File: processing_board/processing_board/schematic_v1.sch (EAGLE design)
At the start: 20 parts, among them Q1 BSS138, Q2 BSS138

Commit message: modified shcematic and board
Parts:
- added J3: (no value), SparkFun-Connectors:CONN_04PTH
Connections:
- removed net N$11: Q2.S, R3.1
- removed net N$2: Q1.S, R2.1
- removed net VDD: C2.1, C3.2, U$1.VIN
- new net CAN_RX: J3.3, Q1.S, R2.1
- new net CAN_TX: J3.2, Q2.S, R3.1
- net +5V: now also C2.1, C3.2, J3.1, U$1.VIN
- net GND: now also J3.4
- net TEENSY_3.3V: now also U$1.3.3V
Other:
- note added: "Level converters from CAN controller to CAN transiever"
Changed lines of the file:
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@@
 <part name="PWR6" library="supply" deviceset="+5V" device=""/>
 <part name="PWR7" library="supply" deviceset="+5V" device=""/>
+<part name="PWR8" library="supply" deviceset="+5V" device=""/>
+<part name="J3" library="SparkFun-Connectors" deviceset="CONN_04" device="PTH"/>
+<part name="GND8" library="supply" deviceset="GND" device=""/>
+<part name="PWR9" library="supply" deviceset="+5V" device=""/>
 </parts>
 <sheets>
@@
 <plain>
 <text x="62.23" y="63.5" size="1.778" layer="91">Supply Decoupling</text>
+<text x="-96.52" y="30.48" size="1.778" layer="91">Level converters from CAN controller to CAN transiever</text>
 </plain>
 <instances>
@@
 <instance part="PWR6" gate="G$1" x="-86.36" y="93.98" smashed="yes"/>
 <instance part="PWR7" gate="G$1" x="-88.9" y="63.5" smashed="yes" rot="R90"/>
+<instance part="PWR8" gate="G$1" x="60.96" y="73.66" smashed="yes" rot="R270"/>
+<instance part="J3" gate="J1" x="-121.92" y="55.88" smashed="yes">
+<attribute name="VALUE" x="-127" y="48.514" size="1.778" layer="96" font="vector"/>
+<attribute name="NAME" x="-127" y="64.008" size="1.778" layer="95" font="vector"/>
+</instance>
+<instance part="GND8" gate="VR1" x="-109.22" y="68.58" smashed="yes" rot="R180"/>
+<instance part="PWR9" gate="G$1" x="-109.22" y="45.72" smashed="yes" rot="R180"/>
 </instances>
 <busses>
 </busses>
 <nets>
-<net name="VDD" class="0">
-<segment>
-<pinref part="C3" gate="G$1" pin="2"/>
-<wire x1="55.88" y1="54.356" x2="55.88" y2="53.34" width="0.1524" layer="91"/>
-<wire x1="55.88" y1="53.34" x2="55.88" y2="45.72" width="0.1524" layer="91"/>
-<wire x1="63.5" y1="45.72" x2="55.88" y2="45.72" width="0.1524" layer="91"/>
-<pinref part="C2" gate="G$1" pin="1"/>
-<wire x1="62.738" y1="54.356" x2="55.88" y2="54.356" width="0.1524" layer="91"/>
-<pinref part="U$1" gate="G$1" pin="VIN"/>
-<wire x1="44.45" y1="68.58" x2="55.88" y2="68.58" width="0.1524" layer="91"/>
-<wire x1="55.88" y1="68.58" x2="55.88" y2="54.356" width="0.1524" layer="91"/>
-</segment>
-</net>
 <net name="GND" class="0">
 <segment>
@@
 <wire x1="200.66" y1="45.72" x2="200.66" y2="48.26" width="0.1524" layer="91"/>
 </segment>
+<segment>
+<pinref part="J3" gate="J1" pin="4"/>
+<wire x1="-116.84" y1="60.96" x2="-109.22" y2="60.96" width="0.1524" layer="91"/>
+<wire x1="-109.22" y1="60.96" x2="-109.22" y2="66.04" width="0.1524" layer="91"/>
+<pinref part="GND8" gate="VR1" pin="GND"/>
+</segment>
 </net>
 <net name="+15V" class="0">
@@
 <wire x1="-88.9" y1="63.5" x2="-86.36" y2="63.5" width="0.1524" layer="91"/>
 </segment>
+<segment>
+<pinref part="PWR8" gate="G$1" pin="+5V"/>
+<wire x1="60.96" y1="73.66" x2="58.42" y2="73.66" width="0.1524" layer="91"/>
+<wire x1="58.42" y1="73.66" x2="58.42" y2="68.58" width="0.1524" layer="91"/>
+<pinref part="C3" gate="G$1" pin="2"/>
+<wire x1="55.88" y1="54.356" x2="55.88" y2="45.72" width="0.1524" layer="91"/>
+<wire x1="63.5" y1="45.72" x2="55.88" y2="45.72" width="0.1524" layer="91"/>
+<pinref part="C2" gate="G$1" pin="1"/>
+<wire x1="62.738" y1="54.356" x2="55.88" y2="54.356" width="0.1524" layer="91"/>
+<pinref part="U$1" gate="G$1" pin="VIN"/>
+<wire x1="44.45" y1="68.58" x2="53.34" y2="68.58" width="0.1524" layer="91"/>
+<wire x1="53.34" y1="68.58" x2="55.88" y2="68.58" width="0.1524" layer="91"/>
+<wire x1="55.88" y1="68.58" x2="55.88" y2="54.356" width="0.1524" layer="91"/>
+<wire x1="58.42" y1="68.58" x2="55.88" y2="68.58" width="0.1524" layer="91"/>
+</segment>
+<segment>
+<pinref part="J3" gate="J1" pin="1"/>
+<wire x1="-116.84" y1="53.34" x2="-109.22" y2="53.34" width="0.1524" layer="91"/>
+<wire x1="-109.22" y1="53.34" x2="-109.22" y2="45.72" width="0.1524" layer="91"/>
+<pinref part="PWR9" gate="G$1" pin="+5V"/>
+</segment>
 </net>
 <net name="+3.3V" class="0">
@@
 </segment>
 </net>
-<net name="N$2" class="0">
+<net name="CAN_RX" class="0">
 <segment>
 <pinref part="R2" gate="G$1" pin="1"/>
@@
 <wire x1="-86.36" y1="68.58" x2="-96.52" y2="68.58" width="0.1524" layer="91"/>
 <junction x="-86.36" y="68.58"/>
+<pinref part="J3" gate="J1" pin="3"/>
+<wire x1="-116.84" y1="58.42" x2="-96.52" y2="58.42" width="0.1524" layer="91"/>
+<wire x1="-96.52" y1="58.42" x2="-96.52" y2="68.58" width="0.1524" layer="91"/>
+<label x="-99.06" y="60.96" size="1.778" layer="95" rot="R180"/>
 </segment>
 </net>
@@
 <label x="-63.5" y="60.96" size="1.778" layer="95"/>
 </segment>
-</net>
-<net name="N$11" class="0">
+<segment>
+<pinref part="U$1" gate="G$1" pin="3.3V"/>
+<wire x1="-1.27" y1="30.48" x2="-10.16" y2="30.48" width="0.1524" layer="91"/>
+<label x="-10.16" y="30.48" size="1.778" layer="95" rot="R180"/>
+</segment>
+</net>
+<net name="CAN_TX" class="0">
 <segment>
 <pinref part="R3" gate="G$1" pin="1"/>
@@
 <wire x1="-86.36" y1="40.64" x2="-96.52" y2="40.64" width="0.1524" layer="91"/>
 <junction x="-86.36" y="40.64"/>
-</segment>
-</net>
+<wire x1="-96.52" y1="40.64" x2="-96.52" y2="55.88" width="0.1524" layer="91"/>
+<pinref part="J3" gate="J1" pin="2"/>
+<wire x1="-96.52" y1="55.88" x2="-116.84" y2="55.88" width="0.1524" layer="91"/>
+<label x="-99.06" y="55.88" size="1.778" layer="95" rot="R180"/>
+</segment>
+</net>

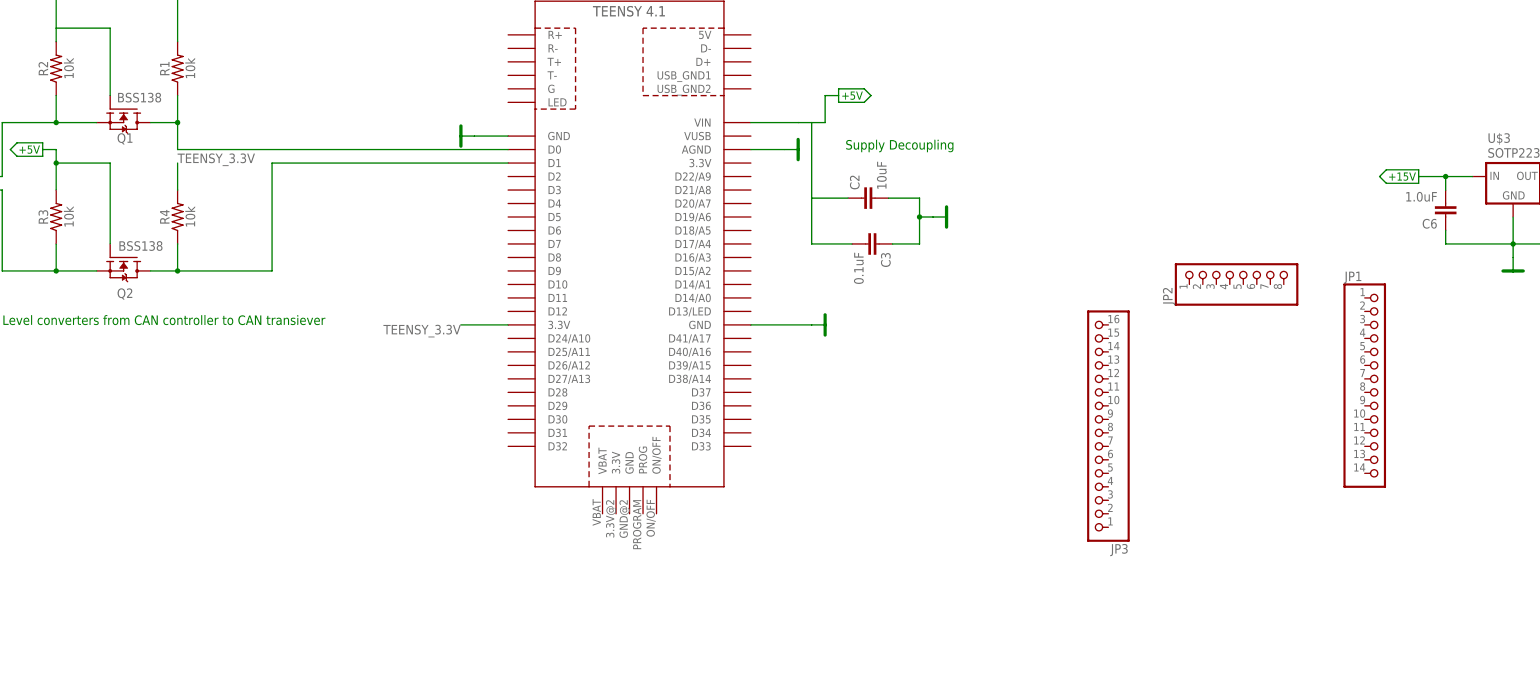
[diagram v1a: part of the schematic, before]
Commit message: routed to radio mod
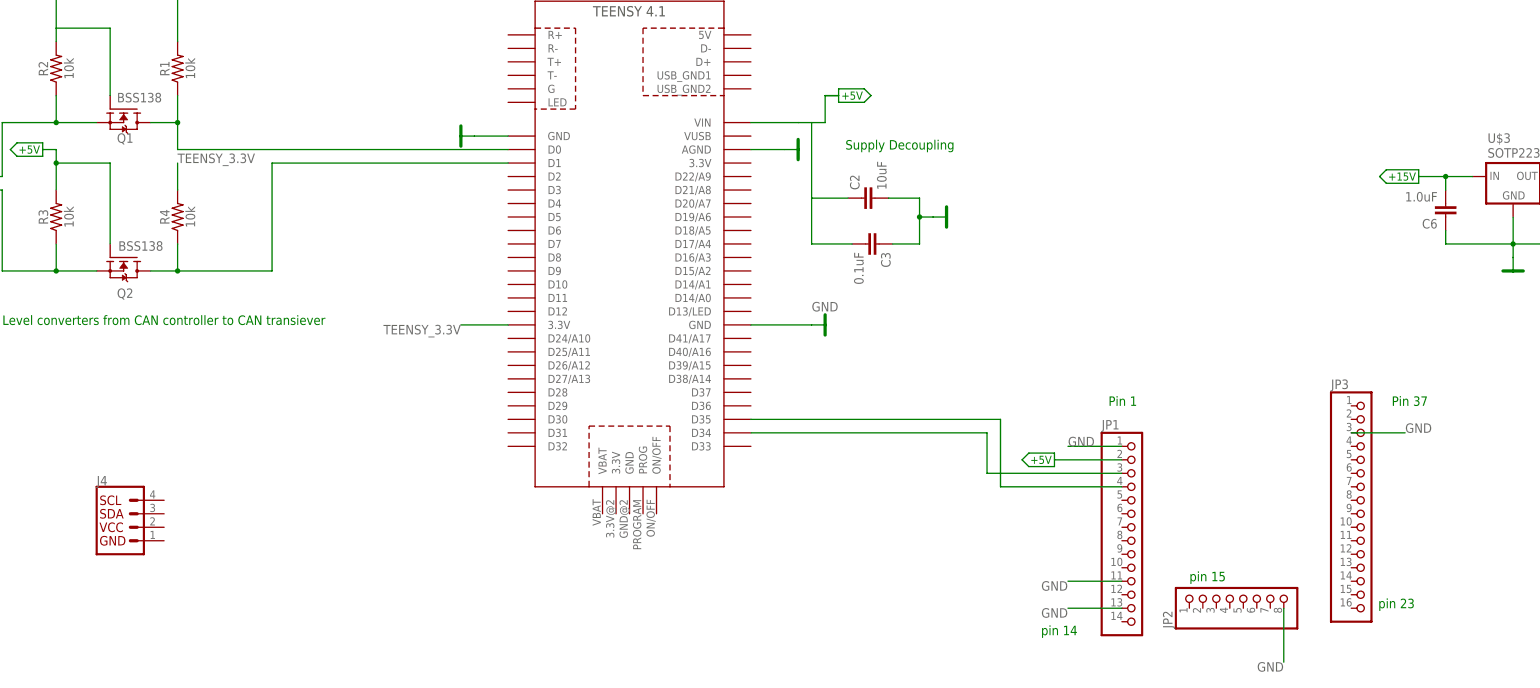
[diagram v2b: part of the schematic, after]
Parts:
- added J4: (no value), SparkFun-Connectors:I2C_STANDARD
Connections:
- new net N$1: JP1.4, U$1.D35
- new net N$2: JP1.3, U$1.D34
- net +5V: now also JP1.2
- net GND: now also JP1.1, JP1.11, JP1.13, JP2.8, JP3.3
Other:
- note added: "Pin 1"
- note added: "Pin 37"
- note added: "pin 14"
- note added: "pin 15"
- note added: "pin 23"
- moved on the sheet: JP1, JP2, JP3
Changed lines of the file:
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@@
 <part name="JP1" library="pinhead" library_urn="urn:adsk.eagle:library:325" deviceset="PINHD-1X14" device="" package3d_urn="urn:adsk.eagle:package:22417/2"/>
 <part name="JP2" library="pinhead" library_urn="urn:adsk.eagle:library:325" deviceset="PINHD-1X8" device="" package3d_urn="urn:adsk.eagle:package:22409/2"/>
-<part name="JP3" library="pinhead" library_urn="urn:adsk.eagle:library:325" deviceset="PINHD-1X16" device="" package3d_urn="urn:adsk.eagle:package:22432/2"/>
 <part name="GND1" library="supply" deviceset="GND" device=""/>
 <part name="J1" library="SparkFun-Connectors" deviceset="BANANA_CONN" device=""/>
@@
 <part name="GND8" library="supply" deviceset="GND" device=""/>
 <part name="PWR9" library="supply" deviceset="+5V" device=""/>
+<part name="J4" library="SparkFun-Connectors" deviceset="I2C_STANDARD" device=""/>
+<part name="PWR10" library="supply" deviceset="+5V" device=""/>
+<part name="JP3" library="pinhead" library_urn="urn:adsk.eagle:library:325" deviceset="PINHD-1X16" device="" package3d_urn="urn:adsk.eagle:package:22432/2"/>
 </parts>
 <sheets>
@@
 <text x="62.23" y="63.5" size="1.778" layer="91">Supply Decoupling</text>
 <text x="-96.52" y="30.48" size="1.778" layer="91">Level converters from CAN controller to CAN transiever</text>
+<text x="111.76" y="15.24" size="1.778" layer="91">Pin 1</text>
+<text x="165.1" y="15.24" size="1.778" layer="91">Pin 37</text>
+<text x="127" y="-17.78" size="1.778" layer="91">pin 15</text>
+<text x="162.56" y="-22.86" size="1.778" layer="91">pin 23</text>
+<text x="99.06" y="-27.94" size="1.778" layer="91">pin 14</text>
 </plain>
 <instances>
@@
 <attribute name="VALUE" x="44.45" y="92.71" size="1.778" layer="96" align="bottom-right"/>
 </instance>
-<instance part="JP1" gate="A" x="162.56" y="20.32" smashed="yes">
-<attribute name="NAME" x="156.21" y="38.735" size="1.778" layer="95"/>
-<attribute name="VALUE" x="156.21" y="-2.54" size="1.778" layer="96"/>
-</instance>
-<instance part="JP2" gate="A" x="137.16" y="40.64" smashed="yes" rot="R90">
-<attribute name="NAME" x="123.825" y="34.29" size="1.778" layer="95" rot="R90"/>
-<attribute name="VALUE" x="149.86" y="34.29" size="1.778" layer="96" rot="R90"/>
-</instance>
-<instance part="JP3" gate="A" x="109.22" y="10.16" smashed="yes" rot="R180">
-<attribute name="NAME" x="115.57" y="-10.795" size="1.778" layer="95" rot="R180"/>
-<attribute name="VALUE" x="115.57" y="35.56" size="1.778" layer="96" rot="R180"/>
+<instance part="JP1" gate="A" x="116.84" y="-7.62" smashed="yes">
+<attribute name="NAME" x="110.49" y="10.795" size="1.778" layer="95"/>
+<attribute name="VALUE" x="110.49" y="-30.48" size="1.778" layer="96"/>
+</instance>
+<instance part="JP2" gate="A" x="137.16" y="-20.32" smashed="yes" rot="R90">
+<attribute name="NAME" x="123.825" y="-26.67" size="1.778" layer="95" rot="R90"/>
+<attribute name="VALUE" x="149.86" y="-26.67" size="1.778" layer="96" rot="R90"/>
 </instance>
 <instance part="GND1" gate="VR1" x="58.42" y="30.48" smashed="yes" rot="R90"/>
@@
 <instance part="GND8" gate="VR1" x="-109.22" y="68.58" smashed="yes" rot="R180"/>
 <instance part="PWR9" gate="G$1" x="-109.22" y="45.72" smashed="yes" rot="R180"/>
+<instance part="J4" gate="G$1" x="-73.66" y="-7.62" smashed="yes">
+<attribute name="VALUE" x="-78.74" y="-12.954" size="1.778" layer="96" font="vector" align="top-left"/>
+<attribute name="NAME" x="-78.74" y="0.254" size="1.778" layer="95" font="vector"/>
+</instance>
+<instance part="PWR10" gate="G$1" x="101.6" y="5.08" smashed="yes" rot="R90"/>
+<instance part="JP3" gate="A" x="160.02" y="-2.54" smashed="yes">
+<attribute name="NAME" x="153.67" y="18.415" size="1.778" layer="95"/>
+<attribute name="VALUE" x="153.67" y="-27.94" size="1.778" layer="96"/>
+</instance>
 </instances>
 <busses>
@@
 <pinref part="U$1" gate="G$1" pin="GND@1"/>
 <wire x1="55.88" y1="30.48" x2="44.45" y2="30.48" width="0.1524" layer="91"/>
+<label x="55.88" y="33.02" size="1.778" layer="95"/>
 </segment>
 <segment>
@@
 <wire x1="-109.22" y1="60.96" x2="-109.22" y2="66.04" width="0.1524" layer="91"/>
 <pinref part="GND8" gate="VR1" pin="GND"/>
+</segment>
+<segment>
+<wire x1="114.3" y1="7.62" x2="104.14" y2="7.62" width="0.1524" layer="91"/>
+<label x="104.14" y="7.62" size="1.778" layer="95"/>
+<pinref part="JP1" gate="A" pin="1"/>
+</segment>
+<segment>
+<wire x1="114.3" y1="-17.78" x2="104.14" y2="-17.78" width="0.1524" layer="91"/>
+<pinref part="JP1" gate="A" pin="11"/>
+<label x="104.14" y="-17.78" size="1.778" layer="95" rot="R180"/>
+</segment>
+<segment>
+<wire x1="114.3" y1="-22.86" x2="104.14" y2="-22.86" width="0.1524" layer="91"/>
+<pinref part="JP1" gate="A" pin="13"/>
+<label x="104.14" y="-22.86" size="1.778" layer="95" rot="R180"/>
+</segment>
+<segment>
+<wire x1="144.78" y1="-22.86" x2="144.78" y2="-33.02" width="0.1524" layer="91"/>
+<pinref part="JP2" gate="A" pin="8"/>
+<label x="144.78" y="-33.02" size="1.778" layer="95" rot="R180"/>
+</segment>
+<segment>
+<wire x1="157.48" y1="10.16" x2="167.64" y2="10.16" width="0.1524" layer="91"/>
+<pinref part="JP3" gate="A" pin="3"/>
+<label x="167.64" y="10.16" size="1.778" layer="95"/>
 </segment>
 </net>
@@
 <wire x1="55.88" y1="68.58" x2="55.88" y2="54.356" width="0.1524" layer="91"/>
 <wire x1="58.42" y1="68.58" x2="55.88" y2="68.58" width="0.1524" layer="91"/>
+<wire x1="60.96" y1="73.66" x2="58.42" y2="73.66" width="0.1524" layer="91"/>
 </segment>
 <segment>
@@
 <wire x1="-109.22" y1="53.34" x2="-109.22" y2="45.72" width="0.1524" layer="91"/>
 <pinref part="PWR9" gate="G$1" pin="+5V"/>
+</segment>
+<segment>
+<wire x1="114.3" y1="5.08" x2="101.6" y2="5.08" width="0.1524" layer="91"/>
+<pinref part="PWR10" gate="G$1" pin="+5V"/>
+<pinref part="JP1" gate="A" pin="2"/>
 </segment>
 </net>
@@
 </segment>
 </net>
+<net name="N$1" class="0">
+<segment>
+<pinref part="U$1" gate="G$1" pin="D35"/>
+<wire x1="44.45" y1="12.7" x2="91.44" y2="12.7" width="0.1524" layer="91"/>
+<wire x1="91.44" y1="12.7" x2="91.44" y2="0" width="0.1524" layer="91"/>
+<wire x1="91.44" y1="0" x2="114.3" y2="0" width="0.1524" layer="91"/>
+<pinref part="JP1" gate="A" pin="4"/>
+</segment>
+</net>
+<net name="N$2" class="0">
+<segment>
+<pinref part="U$1" gate="G$1" pin="D34"/>
+<wire x1="44.45" y1="10.16" x2="88.9" y2="10.16" width="0.1524" layer="91"/>
+<wire x1="88.9" y1="10.16" x2="88.9" y2="2.54" width="0.1524" layer="91"/>
+<wire x1="88.9" y1="2.54" x2="114.3" y2="2.54" width="0.1524" layer="91"/>
+<pinref part="JP1" gate="A" pin="3"/>
+</segment>
+</net>
